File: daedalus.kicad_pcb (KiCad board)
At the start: 4 copper layers, 2 x 7.5 mm, 106 parts, among them J1 CAN Bus, J2 CAN Bus, J3 I2C 1 Breakout, J4 I2C 1 Breakout, J5 A Terminal, J6 B Terminal, J7 C Terminal, J8 SWD, J9 USB_B_Micro, Q1 AO3401A, SW1 SW_SPDT, U1 XT30, U10 TPH, U11 TPH, U12 TPH, U13 TPH, U14 USBLC6-2SC6, U2 XT30, U3 MP2359DJ-LF-Z, U4 MA700, U5 DRV8323RH, U6 MCP2542, U7 STM32F405RGTx, U8 TPH, U9 TPH, Y1 16MHz

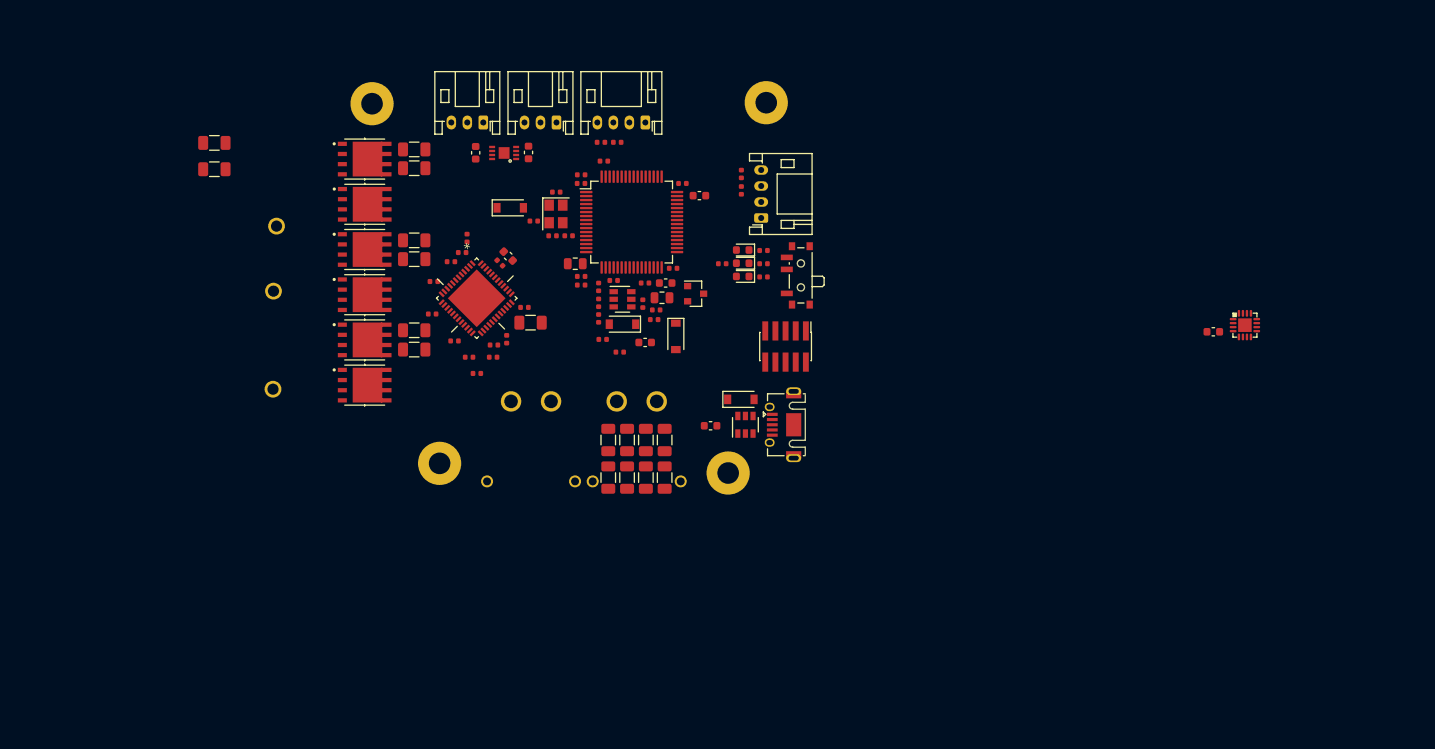
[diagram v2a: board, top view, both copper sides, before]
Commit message: Began sample routing, removed boot switch
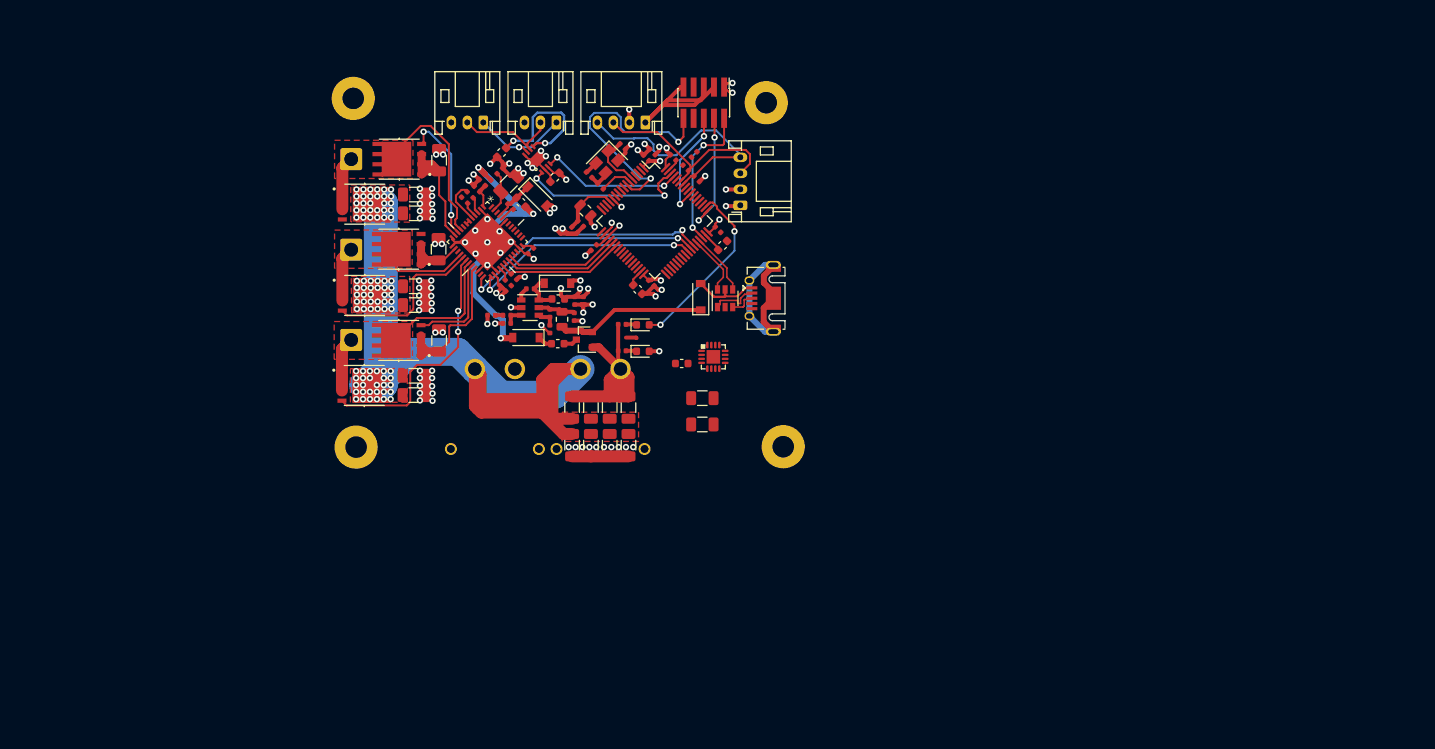
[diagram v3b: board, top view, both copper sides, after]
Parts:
- removed D5: Red, LED_SMD:LED_0603_1608Metric
- removed R10, R11: 2k2, Resistor_SMD:R_0402_1005Metric
- removed R16: 1k, Resistor_SMD:R_0402_1005Metric
- removed SW1: SW_SPDT, Button_Switch_SMD:SW_SPDT_PCM12
- J5, J6, J7: footprint daedalus_kicad_lib:18_AWG_PAD -> Connector_Wire:SolderWire-1sqmm_1x01_D1.4mm_OD2.7mm
- R19, R20, R21: footprint Resistor_SMD:R_0402_1005Metric -> Resistor_SMD:R_1206_3216Metric
- moved C32 68.8 mm to (151.6, 98.0)
- moved C33 68.8 mm to (151.6, 101.3)
- moved C11 66.6 mm to (149.0, 93.7)
- moved U4 66.6 mm to (153.0, 92.9)
- moved J8 32.1 mm to (151.8, 61.1)
- moved C15 23.3 mm to (126.3, 69.6), turned to 225 degrees
- moved F1 21.7 mm to (133.5, 91.2)
- moved R18 21.7 mm to (141.6, 92.1), turned to 0 degrees
- moved C21 20.4 mm to (121.8, 72.6), turned to 45 degrees
- moved J5 19.1 mm to (107.7, 68.1)
- moved D1 18.7 mm to (129.5, 90.4), turned to 180 degrees
- moved R17 18.7 mm to (141.6, 88.8), turned to 0 degrees
- moved D7 17.8 mm to (144.2, 92.2), turned to 0 degrees
- moved C14 17.5 mm to (127.4, 71.2), turned to 225 degrees
- moved J9 16.0 mm to (160.5, 85.5)
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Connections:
- R15 pad 1: Net-(D5-Pad2) -> VDD
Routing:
- net BGND: track 0.00 -> 172.1 mm, vias 0 -> 86
- net VIN: track 0.00 -> 141.1 mm, vias 0 -> 86
- net VDD: track 0.00 -> 41.9 mm, vias 0 -> 21
- net +5VD: track 0.00 -> 36.2 mm, vias 0 -> 3
- net NRST: track 0.00 -> 32.1 mm, vias 0 -> 2
- net I2C1_SCL: track 0.00 -> 31.6 mm
- net GHC: track 0.00 -> 31.3 mm, vias 0 -> 2
- net SOB: track 0.00 -> 31.1 mm, vias 0 -> 2
- net SOA: track 0.00 -> 29.2 mm, vias 0 -> 2
- net PHASE_A: track 0.00 -> 28.1 mm
- net I2C1_SDA: track 0.00 -> 26.4 mm
- net PHASE_C: track 0.00 -> 23.5 mm
- net LED_STATUS: track 0.00 -> 22.8 mm, vias 0 -> 2
- net Net-(J9-Pad6): track 0.00 -> 22.1 mm
- net CAN1_TX: track 0.00 -> 21.9 mm, vias 0 -> 2
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- added copper zone on In1.Cu-GND, net BGND
- added copper zone on F.Cu, net PHASE_A
- added copper zone on F.Cu, net PHASE_B
- added copper zone on F.Cu, net PHASE_C
- added copper zone on In2.Cu-3V3, net VDD
- added copper zone on F.Cu, net VIN
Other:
- outline, holes or cut-outs redrawn

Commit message: Updated footprint and routing
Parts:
- removed J3, J4: I2C 1 Breakout, Connector_JST:JST_PH_S4B-PH-K_1x04_P2.00mm_Horizontal
- J1, J2: footprint Connector_JST:JST_PH_S3B-PH-K_1x03_P2.00mm_Horizontal -> Connector_JST:JST_PH_S3B-PH-SM4-TB_1x03-1MP_P2.00mm_Horizontal
- moved J1 41.3 mm to (137.5, 104.7), turned to 0 degrees
- moved J2 41.1 mm to (124.3, 104.7), turned to 0 degrees
- moved J9 37.3 mm to (131.5, 62.1), turned to 180 degrees
- moved D2 36.6 mm to (123.6, 61.5), turned to 0 degrees
- moved U6 31.1 mm to (131.4, 98.7), turned to 180 degrees
- moved J8 30.2 mm to (143.9, 90.2), turned to 90 degrees
- moved D7 29.6 mm to (140.2, 62.9), turned to 270 degrees
- moved U14 28.9 mm to (131.4, 68.1), turned to 180 degrees
- moved R18 26.7 mm to (140.2, 65.5), turned to 90 degrees
- moved C24 26.6 mm to (126.2, 94.0), turned to 180 degrees
- moved D6 26.6 mm to (138.4, 62.9), turned to 270 degrees
- moved R17 23.6 mm to (138.4, 65.5), turned to 90 degrees
- moved C23 22.8 mm to (128.6, 92.8), turned to 90 degrees
- moved C36 21.3 mm to (116.5, 106.3)
- moved C39 21.3 mm to (114.2, 101.6)
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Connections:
- U7 pad 14: PWM_A -> PWM_C
- U7 pad 16: PWM_C -> PWM_A
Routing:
- net BGND: track 172.1 -> 49.9 mm, vias 86 -> 14
- net VIN: track 141.1 -> 34.8 mm, vias 86 -> 89
- net NRST: track 32.1 -> 0.00 mm, vias 2 -> 0
- net VDD: track 41.9 -> 11.7 mm, vias 21 -> 3
- net I2C1_SCL: track 31.6 -> 1.89 mm
- net ENABLE: track 0.00 -> 26.6 mm, vias 0 -> 4
- net USB_D-: track 7.48 -> 32.9 mm, vias 0 -> 2
- net I2C1_SDA: track 26.4 -> 1.84 mm
- net USB_D+: track 7.85 -> 31.8 mm, vias 0 -> 2
- net LED_STATUS: track 22.8 -> 0.00 mm, vias 2 -> 0
- net CAN1_TX: track 21.9 -> 0.00 mm, vias 2 -> 0
- net GHC: track 31.3 -> 9.52 mm, vias 2 -> 1
- net GHA: track 0.00 -> 18.8 mm, vias 0 -> 2
- net SWDIO: track 18.4 -> 0.00 mm, vias 2 -> 0
- net CAN1_RX: track 17.8 -> 0.00 mm, vias 2 -> 0
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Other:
- board size 2 x 7.5 mm -> 55.9 x 49.7 mm

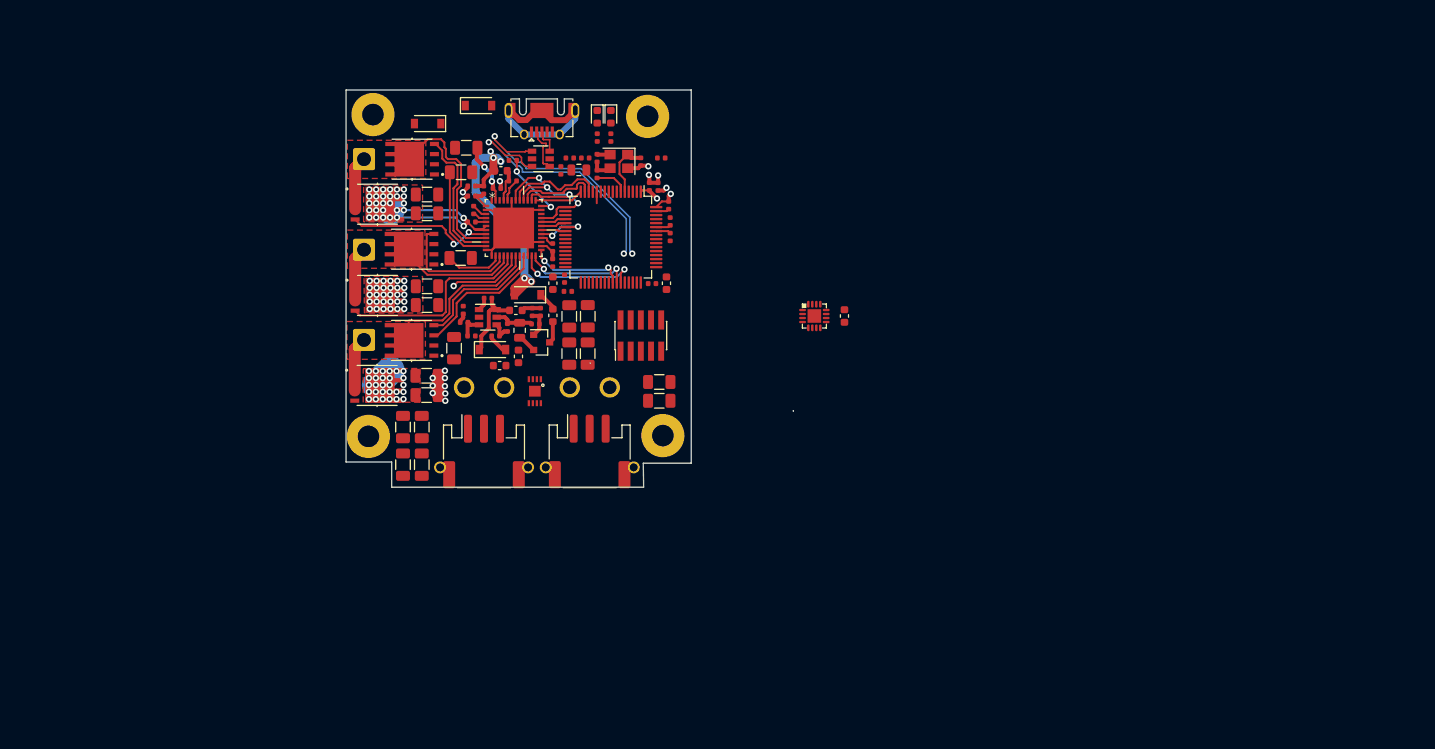
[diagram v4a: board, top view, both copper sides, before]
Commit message: Updated schematic, began v3 layout
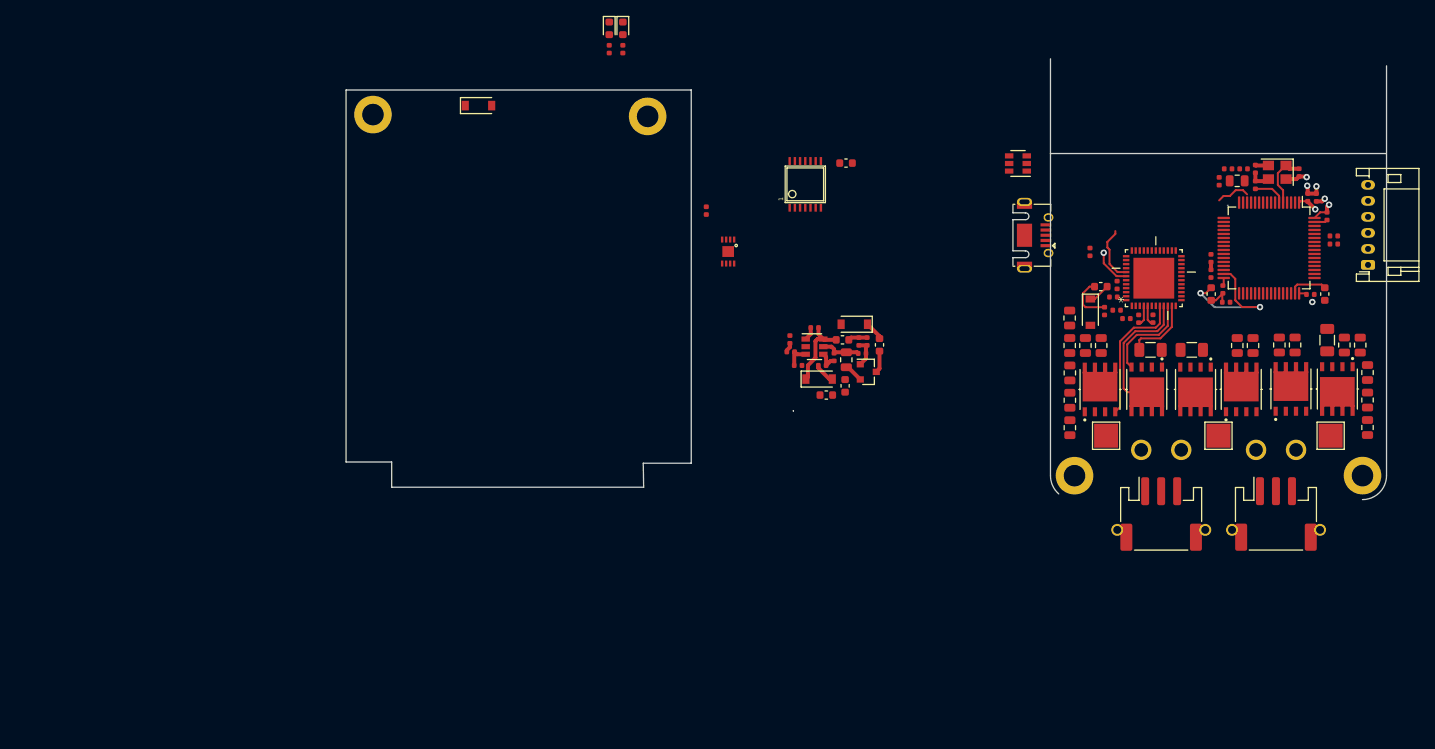
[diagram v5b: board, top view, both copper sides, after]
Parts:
- removed C14: 10uF 50V, Capacitor_SMD:C_1206_3216Metric
- removed J8: SWD, Connector_PinHeader_1.27mm:PinHeader_2x05_P1.27mm_Vertical_SMD
- removed U4: MA700, daedalus_kicad_lib:QFN16
- added 1: AS5147, daedalus_kicad_lib:TSSOP14_as5147, F.Cu at (164.5, 71.3)
- added SWD1: Conn_01x06, Connector_JST:JST_PH_S6B-PH-K_1x06_P2.00mm_Horizontal, F.Cu at (234.8, 81.4)
- C15: value 0.1 uF 50V -> 0.47uF, 50V
- C28, C29, C30, C31, C32, C33, C34, C35, C36, C37, C38, C39, C40, C41, C42, C43: footprint Capacitor_SMD:C_1206_3216Metric -> Capacitor_SMD:C_0805_2012Metric
- H1, H2, H3, H4: footprint MountingHole:MountingHole_2.7mm_M2.5_Pad -> MountingHole:MountingHole_2.7mm_M2.5_DIN965_Pad
- J5, J6, J7: footprint Connector_Wire:SolderWire-1sqmm_1x01_D1.4mm_OD2.7mm -> TestPoint:TestPoint_Pad_3.0x3.0mm
- moved J7 121.4 mm to (230.1, 102.7)
- moved U13 115.9 mm to (231.0, 96.9), turned to 270 degrees
- moved U10 114.2 mm to (225.2, 96.9), turned to 90 degrees
- moved J6 109.3 mm to (216.1, 102.7), turned to 90 degrees
- moved R21 109.1 mm to (229.7, 90.8), turned to 90 degrees
- moved C34 108.7 mm to (225.7, 91.4), turned to 90 degrees
- moved U9 108.6 mm to (218.9, 96.9), turned to 90 degrees
- moved C28 106.7 mm to (223.7, 91.4), turned to 90 degrees
- moved C43 103.4 mm to (220.4, 91.4), turned to 90 degrees
- moved C37 101.6 mm to (218.5, 91.4), turned to 90 degrees
- moved U12 99.6 mm to (213.2, 96.9), turned to 270 degrees
- moved J5 99.0 mm to (202.1, 102.7), turned to 90 degrees
- moved C41 97.7 mm to (234.7, 94.8)
- moved C32 97.0 mm to (231.8, 91.4), turned to 90 degrees
- moved C29 96.6 mm to (233.8, 91.4)
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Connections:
- C11 pad 1: VDD -> BGND
- C11 pad 2: BGND -> VDD
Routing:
- net VIN: track 34.8 -> 0.00 mm, vias 89 -> 0
- net USB_D-: track 32.9 -> 0.00 mm, vias 2 -> 0
- net USB_D+: track 31.8 -> 0.00 mm, vias 2 -> 0
- net BGND: track 49.9 -> 18.4 mm, vias 14 -> 4
- net PHASE_C: track 27.8 -> 0.00 mm
- net +5VD: track 33.2 -> 6.03 mm, vias 5 -> 0
- net GHB: track 25.2 -> 0.00 mm
- net Net-(J9-Pad6): track 22.1 -> 0.00 mm
- net PHASE_B: track 22.0 -> 0.00 mm
- net ENABLE: track 26.6 -> 4.97 mm, vias 4 -> 1
- net Net-(C19-Pad2): track 0.00 -> 17.6 mm, vias 0 -> 2
- net SPC: track 17.3 -> 0.00 mm
- net GLC: track 16.3 -> 0.00 mm
- net SOC: track 15.8 -> 0.00 mm, vias 2 -> 0
- net GLB: track 15.7 -> 0.00 mm
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- removed copper zone on F.Cu, net PHASE_A
- removed copper zone on F.Cu, net PHASE_B
- removed copper zone on F.Cu, net PHASE_C
- removed copper zone on F.Cu, net VIN
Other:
- board size 55.9 x 49.7 mm -> 130.1 x 55.1 mm
- rule via_min_size: 0.4 -> 0.3

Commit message: Finished rough layout v3
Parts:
- 1: moved to B.Cu
- moved SWD1 74.4 mm to (161.4, 93.5)
- moved C25 72.7 mm to (153.9, 77.8)
- moved R14 72.7 mm to (132.5, 96.6), turned to 180 degrees
- moved C16 72.6 mm to (134.0, 96.1)
- moved C21 72.6 mm to (135.8, 96.1)
- moved C28 72.6 mm to (151.6, 99.4)
- moved C29 72.6 mm to (161.7, 99.4)
- moved C31 72.6 mm to (162.6, 109.7)
- moved C32 72.6 mm to (159.7, 99.4)
- moved C34 72.6 mm to (153.5, 99.4)
- moved C35 72.6 mm to (129.3, 99.4)
- moved C38 72.6 mm to (162.6, 106.2)
- moved C39 72.6 mm to (125.4, 109.7)
- moved C41 72.6 mm to (162.6, 102.8)
- moved C42 72.6 mm to (125.4, 99.4)
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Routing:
- net Net-(D1-Pad1): track 2.41 -> 21.4 mm
- net Net-(C19-Pad2): track 17.6 -> 0.00 mm, vias 2 -> 0
- net BGND: track 18.4 -> 6.73 mm, vias 4 -> 1
- net PWM_C: track 11.4 -> 0.00 mm
- net USB_CONN_D-: track 0.00 -> 7.77 mm
- net USB_CONN_D+: track 0.00 -> 7.54 mm
- net HSE_IN: track 7.17 -> 0.00 mm
- net VDD: track 12.0 -> 5.93 mm, vias 3 -> 2
- net BUCK_SW: track 9.65 -> 15.7 mm
- net +5VD: track 6.03 -> 0.00 mm
- net HSE_OUT: track 4.17 -> 0.00 mm
- net Net-(D2-Pad1): track 2.38 -> 6.26 mm
- net Net-(C26-Pad2): track 2.77 -> 0.00 mm
- net SW: track 2.73 -> 0.00 mm
- net Net-(C2-Pad1): track 5.10 -> 4.23 mm
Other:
- board size 130.1 x 55.1 mm -> 52.8 x 50.2 mm
